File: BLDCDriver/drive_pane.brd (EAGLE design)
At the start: 42 x 48.6 mm, 69 parts, among them Q2 SIZ240DT-T1-GE3, Q3 SIZ240DT-T1-GE3, Q4 SIZ240DT-T1-GE3, U1 QFN50P400X400X100-25NDRV8300D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, U2 AS5048A-HTSP-500, U3 MCP2562-E/SN, U4 SOP80P620X125-8N, X2 JST-XH-06-PIN-LONG-PAD

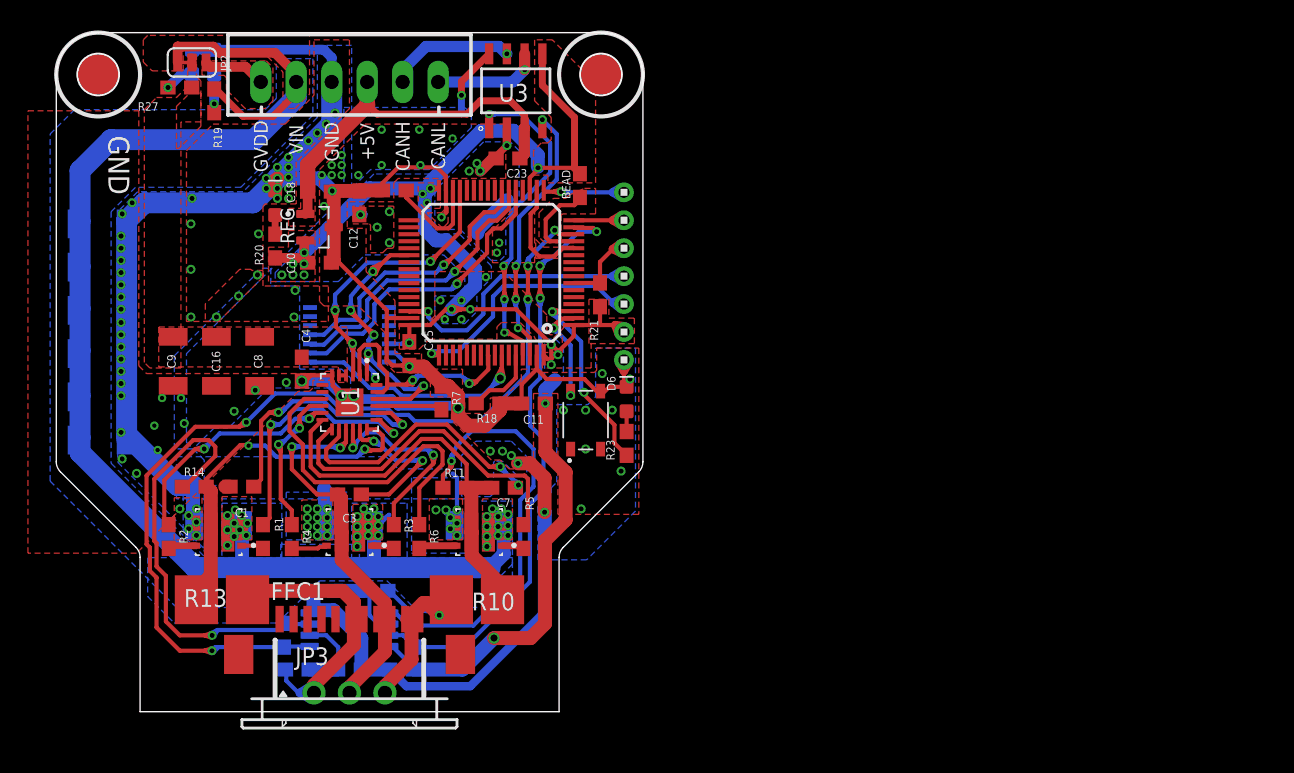
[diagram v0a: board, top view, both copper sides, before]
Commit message: ボードをパネライズした
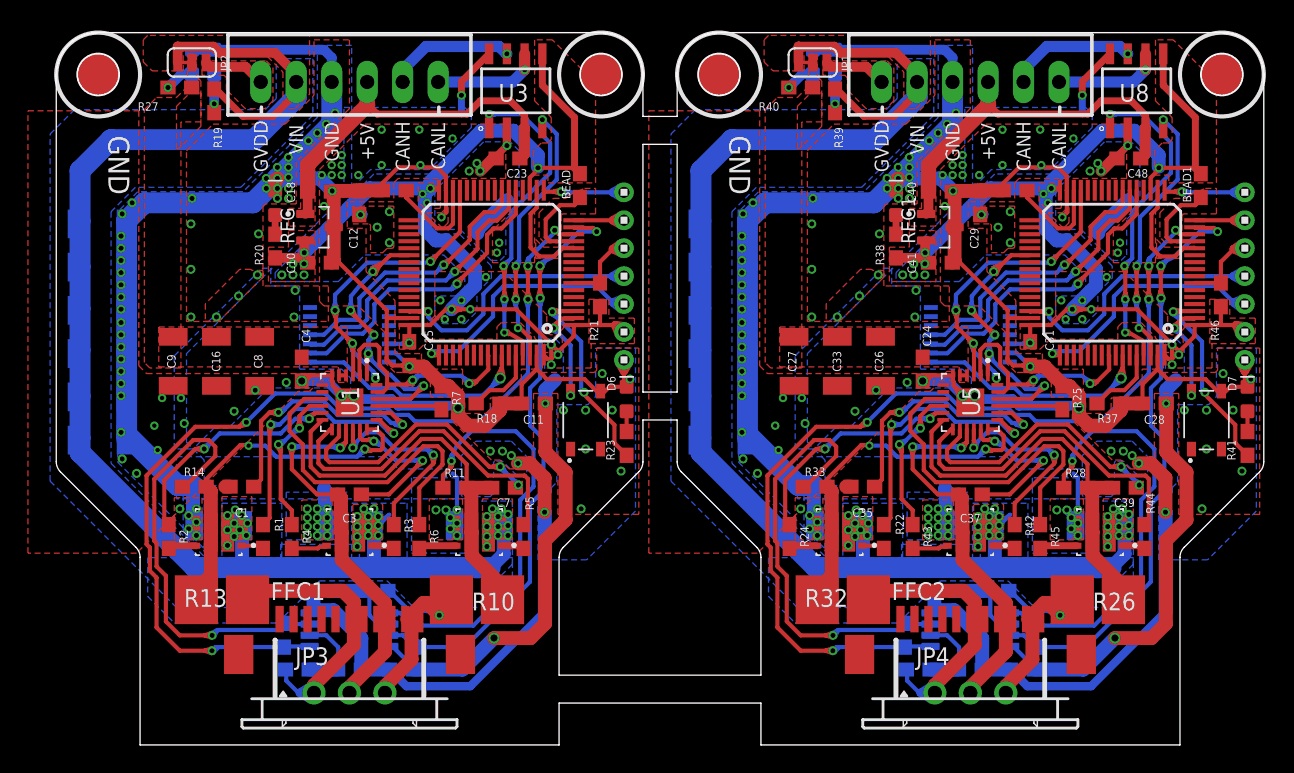
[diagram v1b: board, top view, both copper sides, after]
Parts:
- added BEAD1: 0, SparkFun-Resistors:0603
- added C24, C28, C29, C31, C32, C35, C37, C39, C48: 0.1uF, SparkFun-Capacitors:0603
- added C25, C26, C27, C33, C36, C38, C42, C43, C44, C45, C46, C47: 22UF-1210, SparkFun-Capacitors:1210
- added C30: 4.7uF, SparkFun-Capacitors:0603
- added C40, C41: 0.1UF, Custom_Designed_By_Yusei:1608
- added D4, D7, D8: WHITE, SparkFun-LED:LED-0603
- added D5: RED, SparkFun-LED:LED-0603
- added FFC2: FFC12_11PIN_1MM, MotorDriver_FourthEdition_prot:CON-SMT-FFCFPC_52207-1185
- added JP1: JUMPER-SMT_3_1-NC_TRACE_SILK, SparkFun-Jumpers:SMT-JUMPER_3_1-NC_TRACE_SILK
- added JP4: (no value), adafruit:1X03-CLEANBIG
- added NUCLEO_MAIN1: F446RET6, STM32F446RET6:STM32F446RET6
- added Q1, Q5, Q6: SIZ240DT-T1-GE3, SIZ240DT-T1-GE3:TRANS_SIZ240DT-T1-GE3
- added R22, R24, R42, R43, R44, R45: 50, SparkFun-Resistors:0603
- added R25: 50k, SparkFun-Resistors:0603
- added R26, R32: (no value), resistor-shunt:SMS-REF
- added R28, R29, R33, R34: 1k, SparkFun-Resistors:0603
- added R30, R31, R35, R36: 33k, SparkFun-Resistors:0603
- added R37, R46: 10k, Custom_Designed_By_Yusei:R0603
- added R38: 1k, Custom_Designed_By_Yusei:R0603
- added R39: 10k, SparkFun-Resistors:0603
- added R40: 8k, SparkFun-Resistors:0603
- added R41: 7k, SparkFun-Resistors:0603
- added REG1: AP7333, SOT95P237X112-3N:SOT95P237X112-3N
- added S2: SKRPACE010, Alps SW:SW_SKRPACE010
- added U$4: 1X7, headers(2mm):1X7
- added U$5, U$6: PIN, pin:3MM
- added U5: QFN50P400X400X100-25NDRV8300DRGER, DRV8300DRGER:QFN50P400X400X100-25N
- added U6: AS5048A-HTSP-500, AS5048A-HTSP-500:SOP65P640X120-14N
- added U7: SOP80P620X125-8N, NJM2732:SOP80P620X125-8N
- added U8: MCP2562-E/SN, MCP2562-E_SN:SOIC127P600X175-8N
- added X1: JST-XH-06-PIN-LONG-PAD, Rembrandt Electronics - JST XH Connectors v1-0:JST-XH-06-PACKAGE-LONG-PAD
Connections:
- new net 3V1: BEAD1.2, C28.1, C29.1, C31.1, C32.1, C41.1, NUCLEO_MAIN1.VBAT, NUCLEO_MAIN1.VDD, NUCLEO_MAIN1.VDD1, NUCLEO_MAIN1.VDD2, NUCLEO_MAIN1.VDD3, R38.2, R46.1, REG1.2, U$4.2, U6.12, U7.8, U8.5
- new net 5V1: C40.1, C48.1, REG1.1, U8.3, X1.4
- new net BOOT1: NUCLEO_MAIN1.BOOT0, R37.2
- new net BSTA1: C35.1, U5.BSTA
- new net BSTB1: C37.1, U5.BSTB
- new net BSTC1: C39.1, U5.BSTC
- new net CANH1: U8.7, X1.5
- new net CANL1: U8.6, X1.6
- new net CANRX1: NUCLEO_MAIN1.PB9, U8.4
- new net CANTX1: NUCLEO_MAIN1.PB8, U8.1
- new net CLK1: NUCLEO_MAIN1.PA5, U6.2
- new net CS1: NUCLEO_MAIN1.PB6, U6.1
- new net C_U1: NUCLEO_MAIN1.PA0, R35.1, U7.1
- new net C_W1: NUCLEO_MAIN1.PA1, R30.1, U7.7
- new net DT1: R25.2, U5.DT
- new net GHA1: R22.1, U5.GHA
- new net GHB1: R42.1, U5.GHB
- new net GHC1: R44.1, U5.GHC
- new net GLA1: R24.1, U5.GLA
- new net GLB1: R43.1, U5.GLB
- new net GLC1: R45.1, U5.GLC
- new net GND1: C24.2, C25.1, C26.1, C27.1, C28.2, C29.2, C30.2, C31.2, C32.2, C33.1, C36.1, C38.1, C40.2, C41.2, C42.1, C43.1, C44.1, C45.1, C46.1, C47.1, C48.2, D4.C, D5.C, D7.C, D8.C, NUCLEO_MAIN1.VREF-, NUCLEO_MAIN1.VSS, NUCLEO_MAIN1.VSS1, NUCLEO_MAIN1.VSS2, NUCLEO_MAIN1.VSS3, Q1.5, Q1.6, Q1.7, Q5.5, Q5.6, Q5.7, Q6.5, Q6.6, Q6.7, R25.1, R31.1, R36.1, R37.1, REG1.3, S2.4, U$4.1, U5.GND, U5.PAD, U6.13, U7.4, U8.2, U8.8, X1.3
- new net GVDD1: C24.1, C26.2, C27.2, C33.2, JP1.2, R40.2, U5.GVDD, U5.MODE
- new net GVDD_IN1: JP1.1, X1.1
- new net HA1: Q1.1, R22.2
- new net HB1: Q5.1, R42.2
- new net HC1: Q6.1, R44.2
- new net INA1: NUCLEO_MAIN1.PC7, U5.INHA, U5.INLA
- new net INB1: NUCLEO_MAIN1.PB4, U5.INHB, U5.INLB
- new net INC1: NUCLEO_MAIN1.PB10, U5.INHC, U5.INLC
- new net L1: D8.A, R38.1
- new net LA1: Q1.8, R24.2
- new net LB1: Q5.8, R43.2
- new net LC1: Q6.8, R45.2
- new net LED1: NUCLEO_MAIN1.PC14, R41.2
- new net MISO1: NUCLEO_MAIN1.PA6, U6.3
- new net MOSI1: NUCLEO_MAIN1.PA7, U6.4
- new net N$1: R28.1, R30.2, U7.5
- new net N$2: R29.1, R31.2, U7.6
- new net N$3: R33.1, R35.2, U7.3
- new net N$4: R34.1, R36.2, U7.2
- new net N$5: D4.A, R39.1
- new net N$6: D5.A, R40.1
- new net N$7: D7.A, R41.1
- new net NRST1: NUCLEO_MAIN1.NRST, R46.2, U$4.5
- new net PVDD1: C25.2, C36.2, C38.2, C42.2, C43.2, C44.2, C45.2, C46.2, C47.2, JP1.3, Q1.10, Q1.2, Q1.3, Q1.4, Q5.10, Q5.2, Q5.3, Q5.4, Q6.10, Q6.2, Q6.3, Q6.4, R39.2, X1.2
- new net SW1: NUCLEO_MAIN1.PC13, S2.2
- new net SWCLK1: NUCLEO_MAIN1.PA14, U$4.3
- new net SWDIO1: NUCLEO_MAIN1.PA13, U$4.4
- new net U1: C35.2, Q1.9, R32.2, R33.2, U5.SHA
- new net USBRX1: NUCLEO_MAIN1.PA3, U$4.7
- new net USBTX1: NUCLEO_MAIN1.PA2, U$4.6
- new net U_CS1: FFC2.6, FFC2.7, JP4.1, R32.1, R34.2
- new net V1: C37.2, FFC2.8, FFC2.9, JP4.2, Q5.9, U5.SHB
- new net VCAP1: C30.1, NUCLEO_MAIN1.VCAP_1
- new net VDD5V1: U6.11
- new net VDDA1: BEAD1.1, NUCLEO_MAIN1.VREF+
- new net W1: C39.2, Q6.9, R26.2, R28.2, U5.SHC
- new net W_CS1: FFC2.10, FFC2.11, JP4.3, R26.1, R29.2
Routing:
- net GND1: track 0.00 -> 231.4 mm, vias 0 -> 118
- net 3V1: track 0.00 -> 121.4 mm, vias 0 -> 27
- net PVDD1: track 0.00 -> 116.5 mm, vias 0 -> 34
- net C_U1: track 0.00 -> 76.9 mm, vias 0 -> 5
- net C_W1: track 0.00 -> 48.2 mm, vias 0 -> 3
- net INA1: track 0.00 -> 35.3 mm, vias 0 -> 5
- net N$3: track 0.00 -> 34.0 mm, vias 0 -> 1
- net V1: track 0.00 -> 33.7 mm, vias 0 -> 2
- net N$1: track 0.00 -> 33.0 mm, vias 0 -> 1
- net INC1: track 0.00 -> 32.9 mm, vias 0 -> 4
- net CANTX1: track 0.00 -> 31.7 mm, vias 0 -> 4
- net W1: track 0.00 -> 29.5 mm
- net U1: track 0.00 -> 28.7 mm, vias 0 -> 2
- net 5V1: track 0.00 -> 26.9 mm
- net CLK1: track 0.00 -> 24.8 mm, vias 0 -> 1
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- added copper zone on layer 1, net 3V1
- added copper zone on layer 16, net 3V1
- added copper zone on layer 1, net 5V1
- added copper zone on layer 1, net GND1
- added copper zone on layer 16, net GND1
- added copper zone on layer 1, net GVDD1
- added copper zone on layer 1, net GVDD_IN1
- added copper zone on layer 1, net PVDD1
- added copper zone on layer 16, net PVDD1
- added copper zone on layer 1, net VDDA1
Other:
- board size 42 x 48.6 mm -> 86.5 x 51 mm

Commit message: 発注します
# ==== Emojis ====
# ✨ :sparkles: Add new feature
# ✅  :white_check_mark: Update existing feature (not bug)
# ⚠️  :warning: Fix bug/error
# 🔥  :fire: Remove files or features
# ✏️ :pencil2: Fix typos
# 📝  :memo: Update documentation
# ♻️  :recycle: Dependencies update
# 🐧  :penguin: Improved the Linux
# 🍎  :apple: Improved the macOS
# 🔖 :bookmark: Add new library
# 🎉  :tada: Initial commit

# ==== Format ====
# :emoji: Subject
#
# Commit body...

# ==== Messages ====
# 新規(ファイル)機能追加: Add
# 機能修正、既存機能追加（バグではない): Update
# リファクタリング: Clean
# ファイル名変更:
# 削除など: Remove
# バグ修正: Fix
# バージョンアップ: Upgrade
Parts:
- added U$10, U$7, U$8, U$9: PIN, pin:3MM
- R23, R41: value 7k -> 1k
- U$4: value 1X7 -> PIN; device headers(2mm):1X7 -> pin:3MM
- U$6: value PIN -> 1X7; device pin:3MM -> headers(2mm):1X7
- moved U$4 81.6 mm to (9.60, 4.00), turned to 0 degrees
- moved U$5 66.9 mm to (33.6, 4.00)
- moved U$6 40.3 mm to (85.7, 33.6), turned to 90 degrees
- moved R40 0.72 mm to (53.3, 46.7)
- moved R27 0.72 mm to (8.81, 46.7)
- moved D5 0.32 mm to (54.8, 48.6)
- moved D1 0.32 mm to (11.9, 48.6)
- moved D2 0.32 mm to (10.3, 48.6)
- moved D4 0.32 mm to (56.4, 48.6)
- moved JP2 0.32 mm to (10.3, 48.5)
- moved R19 0.32 mm to (11.9, 45.8)
- moved JP1 0.32 mm to (54.8, 48.5)
- moved R39 0.32 mm to (56.4, 45.8)
- renumbered FFC1 to ., FFC2 to .1
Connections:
- net 3V1: now also U$6.2; no longer U$4.2
- net GND1: now also U$6.1; no longer U$4.1
- net NRST1: now also U$6.5; no longer U$4.5
- net SWCLK1: now also U$6.3; no longer U$4.3
- net SWDIO1: now also U$6.4; no longer U$4.4
- net USBRX1: now also U$6.7; no longer U$4.7
- net USBTX1: now also U$6.6; no longer U$4.6
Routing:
- net CANTX: track 31.7 -> 25.8 mm
- net CANTX1: track 31.7 -> 25.8 mm
- net CANRX1: track 24.2 -> 20.0 mm
- net CANRX: track 24.2 -> 20.0 mm
- net C_U: track 76.9 -> 72.8 mm
- net C_U1: track 76.9 -> 72.8 mm
- net GND: track 231.4 -> 228.6 mm
- net GND1: track 231.4 -> 228.6 mm
- net PVDD1: track 116.5 -> 114.1 mm
- net PVDD: track 116.5 -> 114.1 mm
- net USBRX: track 10.7 -> 8.37 mm
- net USBRX1: track 10.7 -> 8.37 mm
- net N$10: track 34.0 -> 32.1 mm
- net N$3: track 34.0 -> 32.1 mm
- net C_W1: track 48.2 -> 46.8 mm
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- added copper zone on layer 1, net U
- added copper zone on layer 1, net U1
- added copper zone on layer 1, net U_CS
- added copper zone on layer 1, net U_CS1
- added copper zone on layer 1, net V
- added copper zone on layer 1, net V1
- added copper zone on layer 1, net W
- added copper zone on layer 1, net W1
- added copper zone on layer 1, net W_CS
- added copper zone on layer 1, net W_CS1
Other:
- board size 86.5 x 51 mm -> 86.5 x 50 mm
- board text added: "+"
- board text added: "-"
- board text added: "2022"
- board text added: "3V"
- board text added: "Daiki Tomioka"
- board text added: "Designed by"
- board text added: "F446RE"
- board text added: "G"
- board text added: "MD ID"
- board text added: "P"
- board text added: "U"
- board text added: "V"
- board text added: "Version 1.0"
- board text added: "W"
